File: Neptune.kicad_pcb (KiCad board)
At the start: 4 copper layers, 191.2 x 190.9 mm, 379 parts, among them CN2 Expansion, CN3 Cartridge, CN5 1P, CN504 AV Out, CN6 2P, CN7 Barrel_Jack, IC1 68HC000, IC2 LHP6323, IC4 Z80CPU, IC5 LC3664, IC501 SH2 M, IC502 SH2 S, IC503 µPD4502161, IC504 315-5818, IC505 315-5805, IC506 315-5781, IC507 TC511664, IC508 TC511664, IC509 74AC04, IC510 RHSRL33A, IC511 315-5684, IC512 315-5788, IC515 74HC74, IC516 74LS00, IC6 315-5660, IC601 74ACT241, IC7 MSM54C864, IC701 PIC16F630/18324, IC801 TPS564257DRLR, IC901 TL972, IC951 THS7374, J2 EXT, Q801 MMBT3904, X501 *3

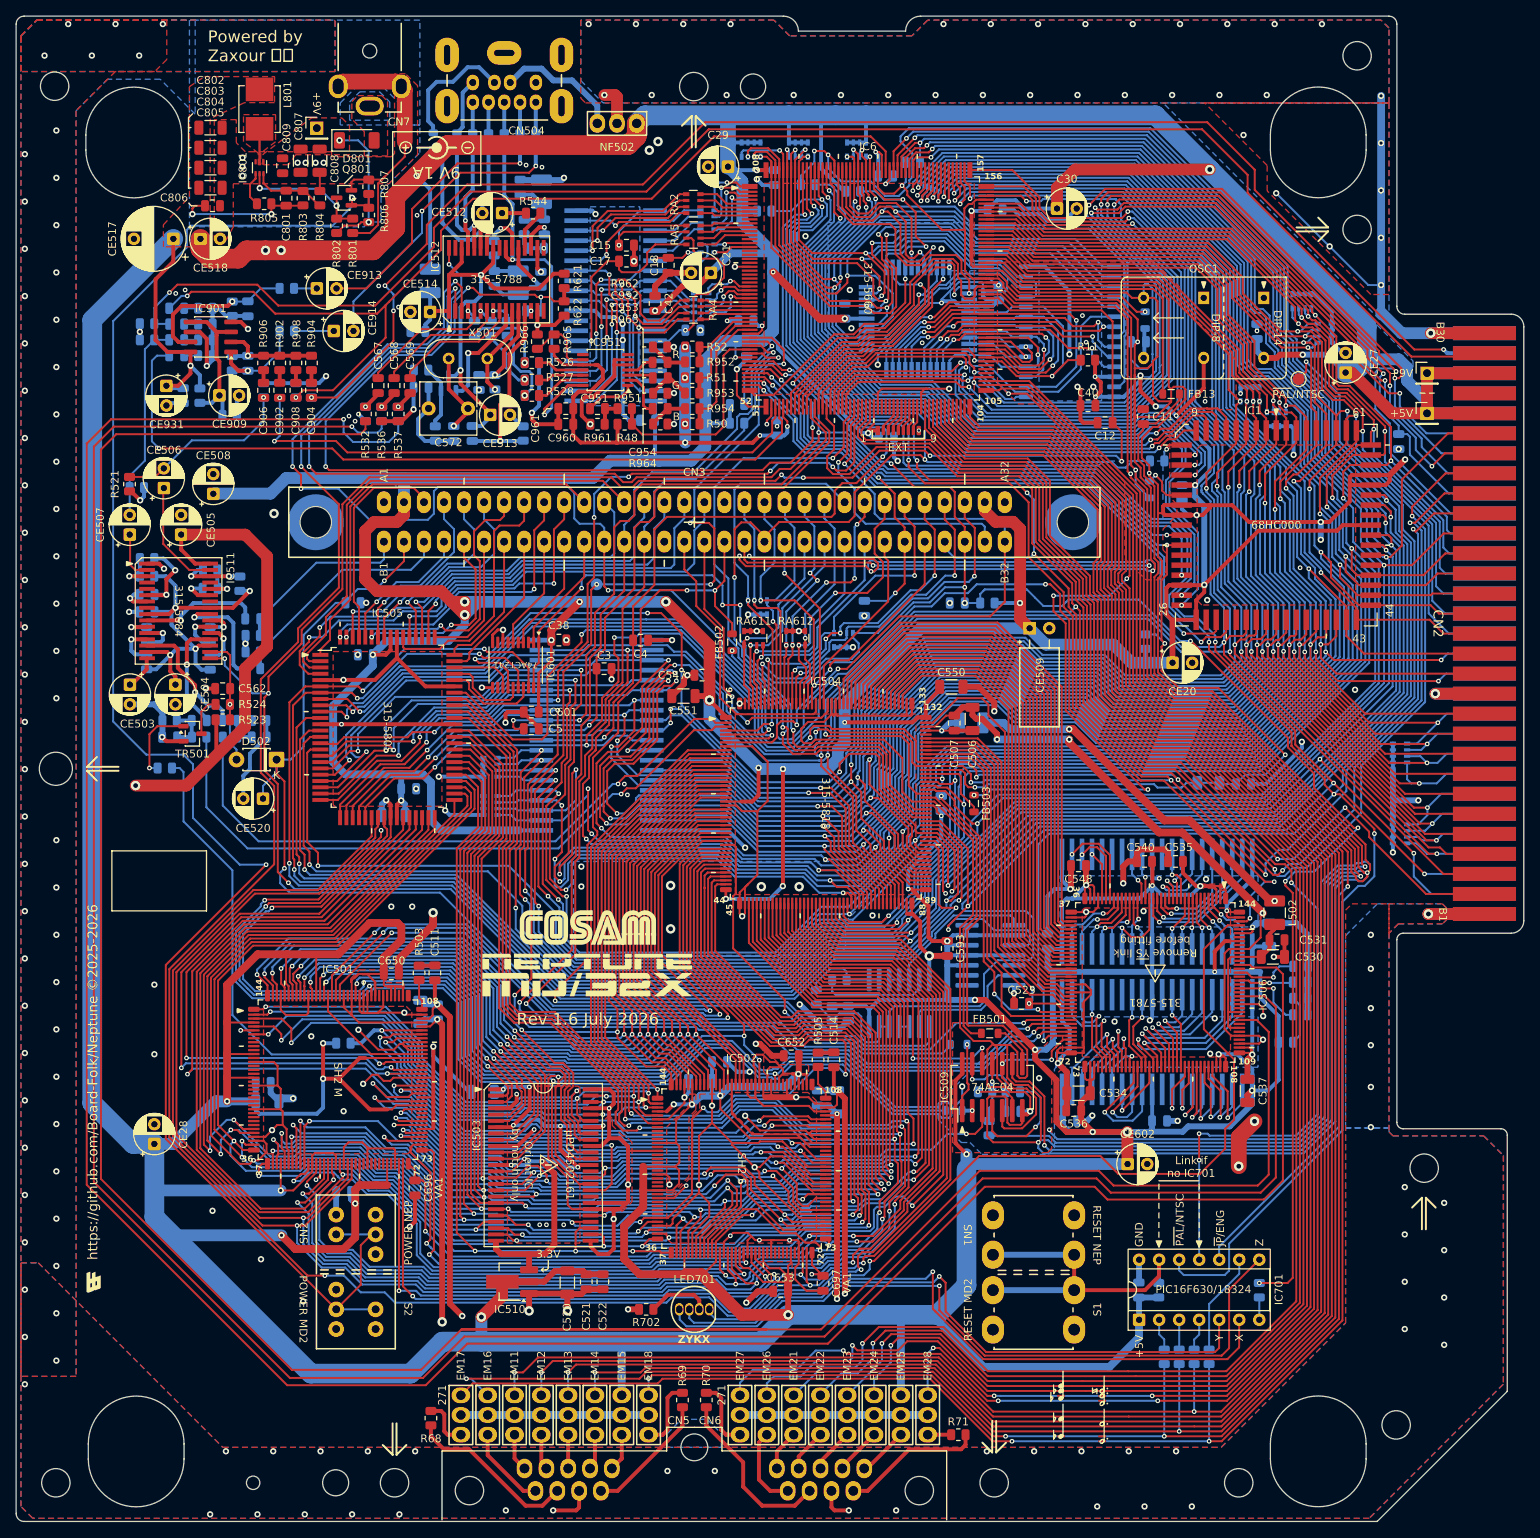
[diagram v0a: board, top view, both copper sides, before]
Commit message: Make pin 1 indicators more consistent.
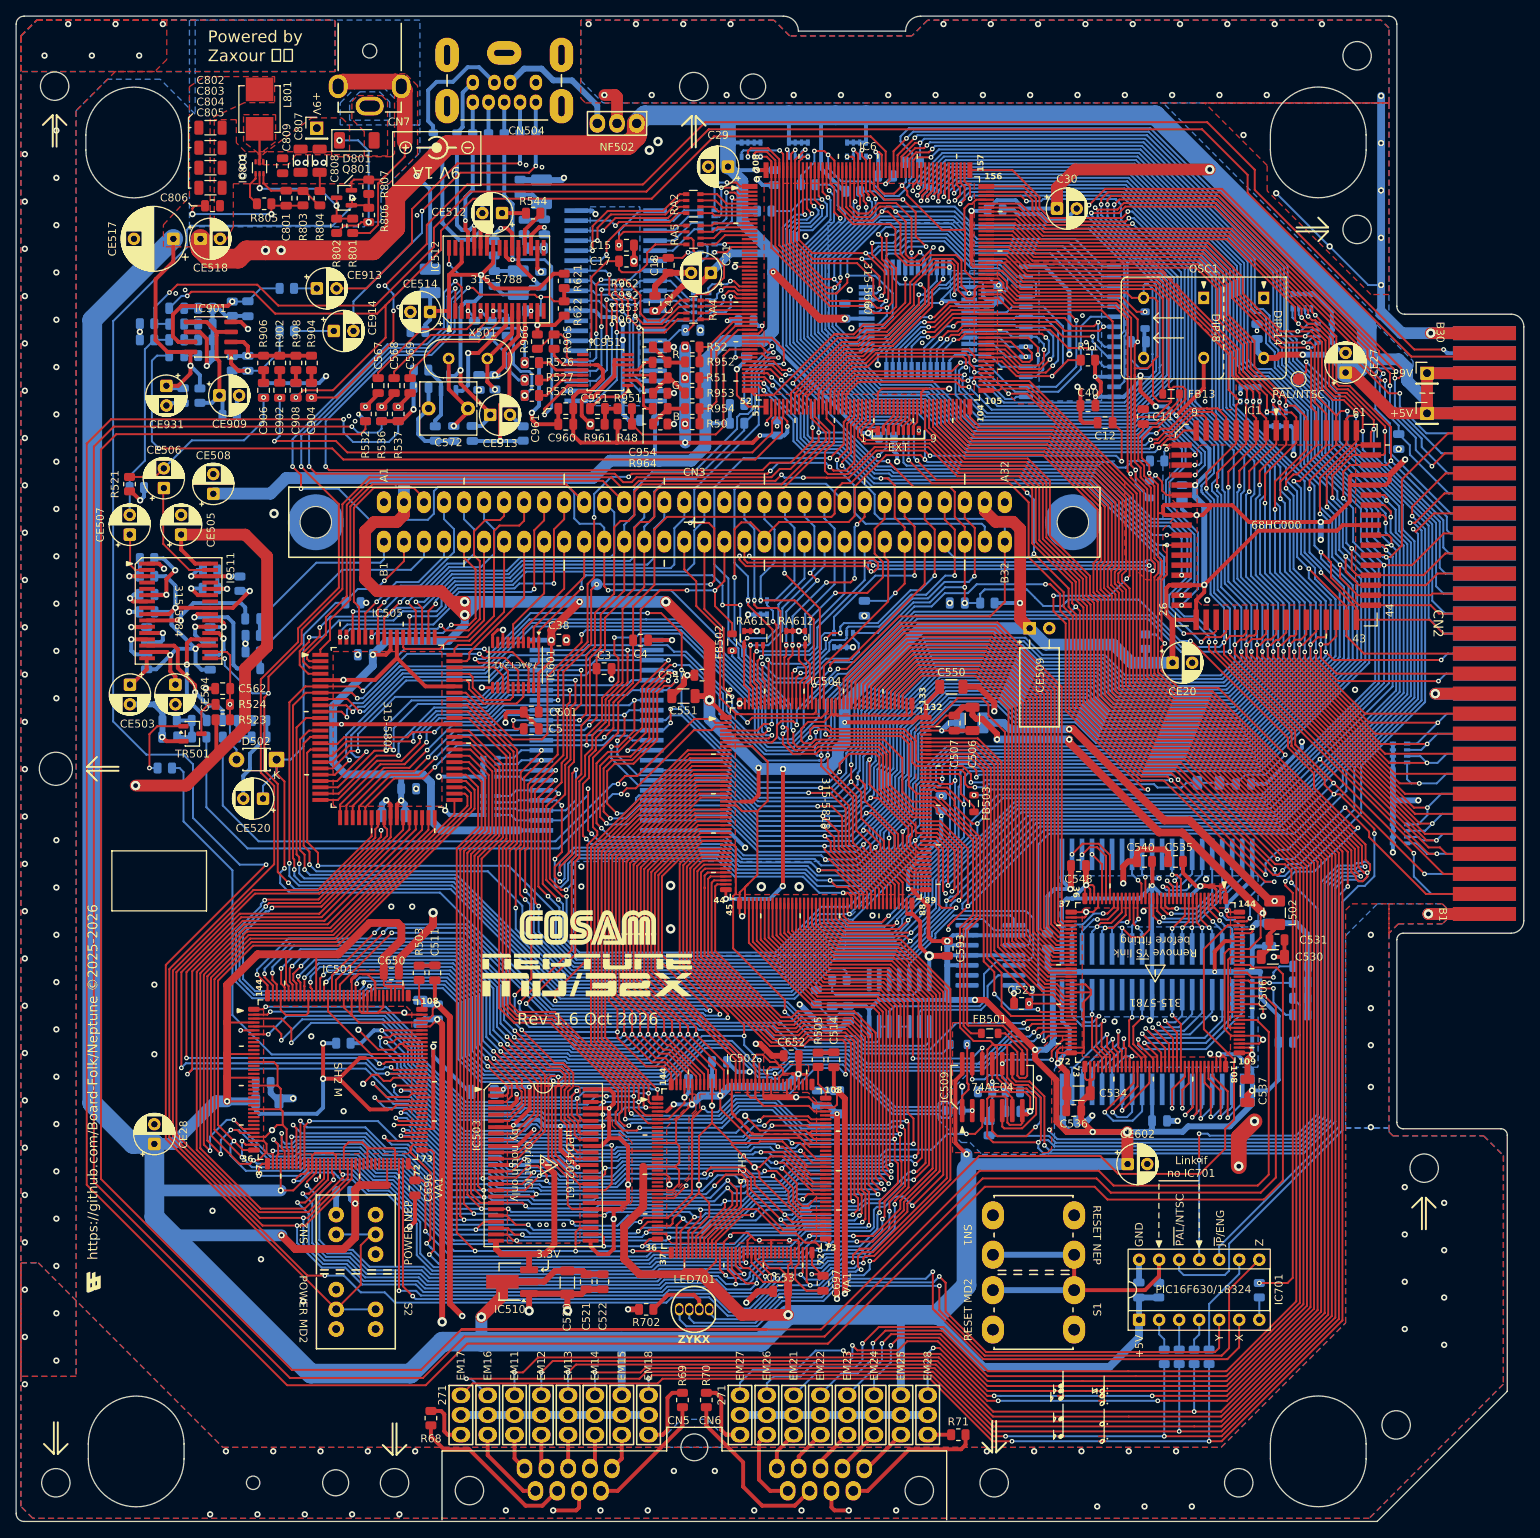
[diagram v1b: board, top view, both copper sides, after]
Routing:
- net ~{ASEL}: track 250.4 -> 249.7 mm
- net ~{CAS2}: track 230.1 -> 230.7 mm
- net ~{CART}: track 87.5 -> 88.0 mm
- net ~{UWR}: track 302.5 -> 302.0 mm
- net ~{LWR}: track 285.1 -> 284.6 mm
- net GND: vias 341 -> 345
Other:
- board text added: "Rev 1.6 Oct 2026"
- board text removed: "Rev 1.6 July 2026"
